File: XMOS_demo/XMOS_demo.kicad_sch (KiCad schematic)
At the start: 0 parts

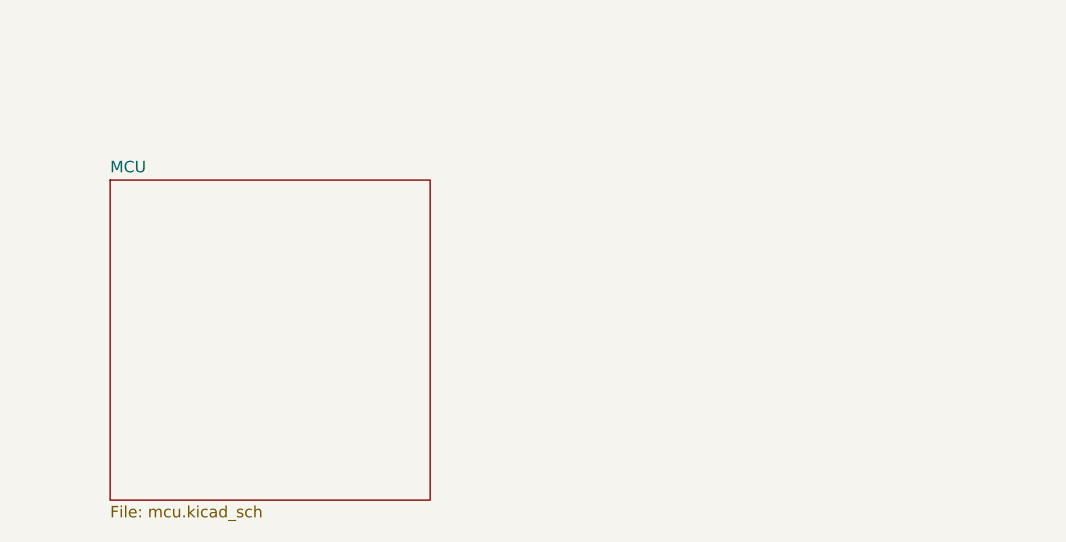
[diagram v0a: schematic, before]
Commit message: usb moved to seperate sch, power supply sch started
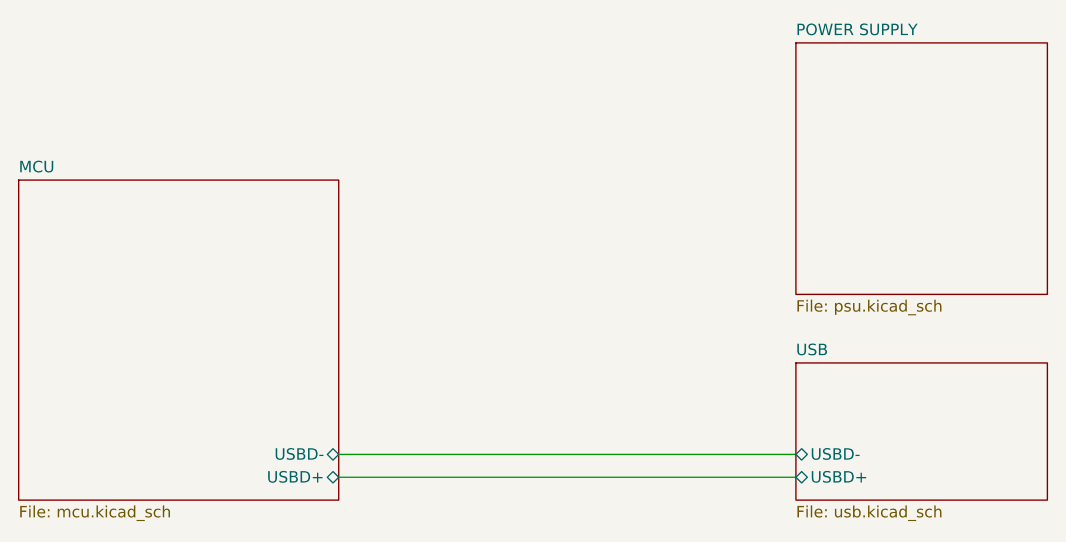
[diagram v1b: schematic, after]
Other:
- added sheet POWER SUPPLY (psu.kicad_sch)
- added sheet USB (usb.kicad_sch)
- sheet MCU ports: added USBD+, USBD-; removed none
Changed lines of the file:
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@@
 	(generator_version "9.0")
 	(paper "A4")
+	(wire
+		(pts
+			(xy 152.4 106.68) (xy 203.2 106.68)
+		)
+		(stroke
+			(width 0)
+			(type default)
+		)
+	)
+	(wire
+		(pts
+			(xy 152.4 109.22) (xy 203.2 109.22)
+		)
+		(stroke
+			(width 0)
+			(type default)
+		)
+	)
 	(sheet
-		(at 127 76.2)
+		(at 203.2 96.52)
+		(size 27.94 15.24)
+		(exclude_from_sim no)
+		(in_bom yes)
+		(on_board yes)
+		(dnp no)
+		(fields_autoplaced yes)
+		(stroke
+			(width 0.1524)
+			(type solid)
+		)
+		(fill
+			(color 0 0 0 0.0000)
+		)
+		(property "Sheetname" "USB"
+			(at 203.2 95.8084 0)
+			(effects
+				(font
+					(size 1.27 1.27)
+				)
+				(justify left bottom)
+			)
+		)
+		(property "Sheetfile" "usb.kicad_sch"
+			(at 203.2 112.3446 0)
+			(effects
+				(font
+					(size 1.27 1.27)
+				)
+				(justify left top)
+			)
+		)
+		(pin "USBD+" bidirectional
+			(at 203.2 109.22 180)
+			(effects
+				(font
+					(size 1.27 1.27)
+				)
+				(justify left)
+			)
+		)
+		(pin "USBD-" bidirectional
+			(at 203.2 106.68 180)
+			(effects
+				(font
+					(size 1.27 1.27)
+				)
+				(justify left)
+			)
+		)
+		(instances
+			(project "XMOS_demo"
+				(path "/0a855fb0-ca19-4770-811e-70d8770d7fdd"
+					(page "3")
+				)
+			)
+		)
+	)
+	(sheet
+		(at 203.2 60.96)
+		(size 27.94 27.94)
+		(exclude_from_sim no)
+		(in_bom yes)
+		(on_board yes)
+		(dnp no)
+		(fields_autoplaced yes)
+		(stroke
+			(width 0.1524)
+			(type solid)
+		)
+		(fill
+			(color 0 0 0 0.0000)
+		)
+		(property "Sheetname" "POWER SUPPLY"
+			(at 203.2 60.2484 0)
+			(effects
+				(font
+					(size 1.27 1.27)
+				)
+				(justify left bottom)
+			)
+		)
+		(property "Sheetfile" "psu.kicad_sch"
+			(at 203.2 89.4846 0)
+			(effects
+				(font
+					(size 1.27 1.27)
+				)
+				(justify left top)
+			)
+		)
+		(instances
+			(project "XMOS_demo"
+				(path "/0a855fb0-ca19-4770-811e-70d8770d7fdd"
+					(page "4")
+				)
+			)
+		)
+	)
+	(sheet
+		(at 116.84 76.2)
 		(size 35.56 35.56)
 		(exclude_from_sim no)
@@
 		)
 		(property "Sheetname" "MCU"
-			(at 127 75.4884 0)
+			(at 116.84 75.4884 0)
 			(effects
 				(font
@@
 		)
 		(property "Sheetfile" "mcu.kicad_sch"
-			(at 127 112.3446 0)
+			(at 116.84 112.3446 0)
 			(effects
 				(font
@@
 			)
 		)
+		(pin "USBD+" bidirectional
+			(at 152.4 109.22 0)
+			(effects
+				(font
+					(size 1.27 1.27)
+				)
+				(justify right)
+			)
+		)
+		(pin "USBD-" bidirectional
+			(at 152.4 106.68 0)
+			(effects
+				(font
+					(size 1.27 1.27)
+				)
+				(justify right)
+			)
+		)

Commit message: sch work
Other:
- added sheet Audio Out (audio_out.kicad_sch)
- added sheet Codec (codec.kicad_sch)
- company: (none) -> AGH University
- title: (none) -> USB Sound Card Top Level
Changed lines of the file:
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@@
 	(generator_version "9.0")
 	(paper "A4")
+	(title_block
+		(title "USB Sound Card Top Level")
+		(date "2026-03-29")
+		(rev "0.1")
+		(company "AGH University")
+	)
 	(wire
 		(pts
-			(xy 152.4 106.68) (xy 203.2 106.68)
+			(xy 107.95 109.22) (xy 116.84 109.22)
 		)
 		(stroke
@@
 	(wire
 		(pts
-			(xy 152.4 109.22) (xy 203.2 109.22)
+			(xy 107.95 106.68) (xy 116.84 106.68)
 		)
 		(stroke
@@
 	)
 	(sheet
-		(at 203.2 96.52)
+		(at 80.01 96.52)
 		(size 27.94 15.24)
 		(exclude_from_sim no)
@@
 		)
 		(property "Sheetname" "USB"
-			(at 203.2 95.8084 0)
+			(at 80.01 95.8084 0)
 			(effects
 				(font
@@
 		)
 		(property "Sheetfile" "usb.kicad_sch"
-			(at 203.2 112.3446 0)
+			(at 80.01 112.3446 0)
 			(effects
 				(font
@@
 		)
 		(pin "USBD+" bidirectional
-			(at 203.2 109.22 180)
-			(effects
-				(font
-					(size 1.27 1.27)
-				)
-				(justify left)
+			(at 107.95 109.22 0)
+			(effects
+				(font
+					(size 1.27 1.27)
+				)
+				(justify right)
 			)
 		)
 		(pin "USBD-" bidirectional
-			(at 203.2 106.68 180)
-			(effects
-				(font
-					(size 1.27 1.27)
-				)
-				(justify left)
+			(at 107.95 106.68 0)
+			(effects
+				(font
+					(size 1.27 1.27)
+				)
+				(justify right)
 			)
 		)
@@
 	)
 	(sheet
-		(at 203.2 60.96)
+		(at 80.01 55.88)
 		(size 27.94 27.94)
 		(exclude_from_sim no)
@@
 		)
 		(property "Sheetname" "POWER SUPPLY"
-			(at 203.2 60.2484 0)
+			(at 80.01 55.1684 0)
 			(effects
 				(font
@@
 		)
 		(property "Sheetfile" "psu.kicad_sch"
-			(at 203.2 89.4846 0)
+			(at 80.01 84.4046 0)
 			(effects
 				(font
@@
 				(path "/0a855fb0-ca19-4770-811e-70d8770d7fdd"
 					(page "4")
+				)
+			)
+		)
+	)
+	(sheet
+		(at 162.56 76.2)
+		(size 38.1 35.56)
+		(exclude_from_sim no)
+		(in_bom yes)
+		(on_board yes)
+		(dnp no)
+		(fields_autoplaced yes)
+		(stroke
+			(width 0.1524)
+			(type solid)
+		)
+		(fill
+			(color 0 0 0 0.0000)
+		)
+		(property "Sheetname" "Codec"
+			(at 162.56 75.4884 0)
+			(effects
+				(font
+					(size 1.27 1.27)
+				)
+				(justify left bottom)
+			)
+		)
+		(property "Sheetfile" "codec.kicad_sch"
+			(at 162.56 112.3446 0)
+			(effects
+				(font
+					(size 1.27 1.27)
+				)
+				(justify left top)
+			)
+		)
+		(instances
+			(project "XMOS_demo"
+				(path "/0a855fb0-ca19-4770-811e-70d8770d7fdd"
+					(page "6")
+				)
+			)
+		)
+	)
+	(sheet
+		(at 208.28 76.2)
+		(size 30.48 35.56)
+		(exclude_from_sim no)
+		(in_bom yes)
+		(on_board yes)
+		(dnp no)
+		(fields_autoplaced yes)
+		(stroke
+			(width 0.1524)
+			(type solid)
+		)
+		(fill
+			(color 0 0 0 0.0000)
+		)
+		(property "Sheetname" "Audio Out"
+			(at 208.28 75.4884 0)
+			(effects
+				(font
+					(size 1.27 1.27)
+				)
+				(justify left bottom)
+			)
+		)
+		(property "Sheetfile" "audio_out.kicad_sch"
+			(at 208.28 112.3446 0)
+			(effects
+				(font
+					(size 1.27 1.27)
+				)
+				(justify left top)
+			)
+		)
+		(instances
+			(project "XMOS_demo"
+				(path "/0a855fb0-ca19-4770-811e-70d8770d7fdd"
+					(page "5")
 				)
 			)
@@
 		)
 		(pin "USBD+" bidirectional
-			(at 152.4 109.22 0)
-			(effects
-				(font
-					(size 1.27 1.27)
-				)
-				(justify right)
+			(at 116.84 109.22 180)
+			(effects
+				(font
+					(size 1.27 1.27)
+				)
+				(justify left)
 			)
 		)
 		(pin "USBD-" bidirectional
-			(at 152.4 106.68 0)
-			(effects
-				(font
-					(size 1.27 1.27)
-				)
-				(justify right)
-			)
-		)
+			(at 116.84 106.68 180)
+			(effects
+				(font
+					(size 1.27 1.27)
+				)
+				(justify left)
+			)
+		)

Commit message: Lots of sch work
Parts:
- added NT1, NT2, NT3, NT4, NT5: NetTie_2, NetTie:NetTie-2_SMD_Pad0.5mm, symbol Device:NetTie_2
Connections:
- new net Audio Out/INL+: NT4.2
- new net Audio Out/INL-: NT5.2
- new net Audio Out/INR+: NT2.2
- new net Audio Out/INR-: NT3.2
- new net Audio Out/~{SHDN}: NT1.2
- new net Codec/OUT_A+: NT2.1
- new net Codec/OUT_A-: NT3.1
- new net Codec/OUT_B+: NT4.1
- new net Codec/OUT_B-: NT5.1
- new net Codec/~{MUTE}: NT1.1
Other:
- sheet Audio Out ports: added INL+, INL-, INR+, INR-, ~{SHDN}; removed none
- sheet Codec ports: added AIN_A, AIN_B, OUT_A+, OUT_A-, OUT_B+, OUT_B-, VQ1, VQ2, VQ3, ~{MUTE}; removed none
- note added: "TODO: add audio input front end"
- note added: "TODO: add optional low pass filter"

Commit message: sch work, pcb import and initial board outline
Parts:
- added H1, H2, H3, H4: M3_NPTH, MountingHole:MountingHole_3.2mm_M3, symbol Mechanical:MountingHole
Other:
- added sheet Audio In (audio_in.kicad_sch)
- sheet Codec ports: added CODEC_LRCK, CODEC_MCLK, CODEC_SCLK, CODEC_SDIN, CODEC_SDOUT, CODEC_~{RST}, SCL, SDA; removed none
- note added: "TODO: add missing voltage regulators"

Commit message: sch mostly finished, needs tp, pcb component layout started
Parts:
- added TP1, TP2, TP3, TP4: GND, TestPoint:TestPoint_Bridge_Pitch2.54mm_Drill1.0mm, symbol Connector:TestPoint
- renumbered NT2 to NT1, NT3 to NT2, NT4 to NT3, NT5 to NT4, NT1 to NT5
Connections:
- net Audio Out/INL+: now also NT1.2; no longer NT3.2
- net Audio Out/INL-: now also NT2.2; no longer NT4.2
- net Audio Out/INR+: now also NT3.2; no longer NT1.2
- net Audio Out/INR-: now also NT4.2; no longer NT2.2
- new net GND: TP1.1, TP2.1, TP3.1, TP4.1
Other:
- sheet Audio In ports: added AIN_A, AIN_B, VQ1, VQ2, VQ3; removed none
- note removed: "TODO: add audio input front end"
- note removed: "TODO: add missing voltage regulators"

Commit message: finished sch, pcb work
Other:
- sheet Codec ports: added I2S_ADC, I2S_DAC, I2S_LRCK, I2S_SCLK, MCLK; removed CODEC_LRCK, CODEC_MCLK, CODEC_SCLK, CODEC_SDIN, CODEC_SDOUT
- sheet MCU ports: added CODEC_~{RST}, I2S_ADC, I2S_DAC, I2S_LRCK, I2S_SCLK, MCLK, SCL, SDA; removed none
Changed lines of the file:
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@@
+	(wire
+		(pts
+			(xy 119.38 88.9) (xy 129.54 88.9)
+		)
+		(stroke
+			(width 0)
+			(type default)
+		)
+	)
+	(wire
+		(pts
+			(xy 119.38 91.44) (xy 129.54 91.44)
+		)
+		(stroke
+			(width 0)
+			(type default)
+		)
+	)
 	(wire
 		(pts
@@
 	(wire
 		(pts
+			(xy 119.38 109.22) (xy 129.54 109.22)
+		)
+		(stroke
+			(width 0)
+			(type default)
+		)
+	)
+	(wire
+		(pts
 			(xy 167.64 83.82) (xy 175.26 83.82)
 		)
@@
 	(wire
 		(pts
+			(xy 119.38 93.98) (xy 129.54 93.98)
+		)
+		(stroke
+			(width 0)
+			(type default)
+		)
+	)
+	(wire
+		(pts
 			(xy 45.72 129.54) (xy 35.56 129.54)
 		)
@@
 	(wire
 		(pts
+			(xy 119.38 86.36) (xy 129.54 86.36)
+		)
+		(stroke
+			(width 0)
+			(type default)
+		)
+	)
+	(wire
+		(pts
 			(xy 167.64 81.28) (xy 175.26 81.28)
 		)
@@
 	(wire
 		(pts
+			(xy 119.38 106.68) (xy 129.54 106.68)
+		)
+		(stroke
+			(width 0)
+			(type default)
+		)
+	)
+	(wire
+		(pts
+			(xy 119.38 96.52) (xy 129.54 96.52)
+		)
+		(stroke
+			(width 0)
+			(type default)
+		)
+	)
+	(wire
+		(pts
 			(xy 74.93 109.22) (xy 83.82 109.22)
 		)
@@
 		(pts
 			(xy 180.34 78.74) (xy 213.36 78.74)
+		)
+		(stroke
+			(width 0)
+			(type default)
+		)
+	)
+	(wire
+		(pts
+			(xy 119.38 78.74) (xy 129.54 78.74)
 		)
 		(stroke
@@
 		(dnp no)
 		(fields_autoplaced yes)
-		(property "Reference" "#PWR094"
+		(property "Reference" "#PWR01"
 			(at 35.56 138.43 0)
 			(effects
@@
 			(project "XMOS_demo"
 				(path "/0a855fb0-ca19-4770-811e-70d8770d7fdd"
-					(reference "#PWR094")
+					(reference "#PWR01")
 					(unit 1)
 				)
@@
 			)
 		)
-		(pin "CODEC_LRCK" input
+		(pin "I2S_ADC" output
 			(at 129.54 88.9 180)
 			(effects
@@
 			)
 		)
-		(pin "CODEC_MCLK" input
+		(pin "MCLK" input
 			(at 129.54 86.36 180)
 			(effects
@@
 			)
 		)
-		(pin "CODEC_SCLK" input
+		(pin "I2S_SCLK" input
 			(at 129.54 91.44 180)
 			(effects
@@
 			)
 		)
-		(pin "CODEC_SDIN" input
+		(pin "I2S_DAC" input
 			(at 129.54 96.52 180)
 			(effects
@@
 			)
 		)
-		(pin "CODEC_SDOUT" output
+		(pin "I2S_LRCK" input
 			(at 129.54 93.98 180)
 			(effects
@@
 			)
 		)
+		(pin "CODEC_~{RST}" output
+			(at 119.38 78.74 0)
+			(effects
+				(font
+					(size 1.27 1.27)
+				)
+				(justify right)
+			)
+		)
+		(pin "I2S_ADC" input
+			(at 119.38 88.9 0)
+			(effects
+				(font
+					(size 1.27 1.27)
+				)
+				(justify right)
+			)
+		)
+		(pin "I2S_SCLK" output
+			(at 119.38 91.44 0)
+			(effects
+				(font
+					(size 1.27 1.27)
+				)
+				(justify right)
+			)
+		)
+		(pin "I2S_DAC" output
+			(at 119.38 96.52 0)
+			(effects
+				(font
+					(size 1.27 1.27)
+				)
+				(justify right)
+			)
+		)
+		(pin "I2S_LRCK" output
+			(at 119.38 93.98 0)
+			(effects
+				(font
+					(size 1.27 1.27)
+				)
+				(justify right)
+			)
+		)
+		(pin "MCLK" output
+			(at 119.38 86.36 0)
+			(effects
+				(font
+					(size 1.27 1.27)
+				)
+				(justify right)
+			)
+		)
+		(pin "SCL" bidirectional
+			(at 119.38 106.68 0)
+			(effects
+				(font
+					(size 1.27 1.27)
+				)
+				(justify right)
+			)
+		)
+		(pin "SDA" bidirectional
+			(at 119.38 109.22 0)
+			(effects
+				(font
+					(size 1.27 1.27)
+				)
+				(justify right)
+			)
+		)

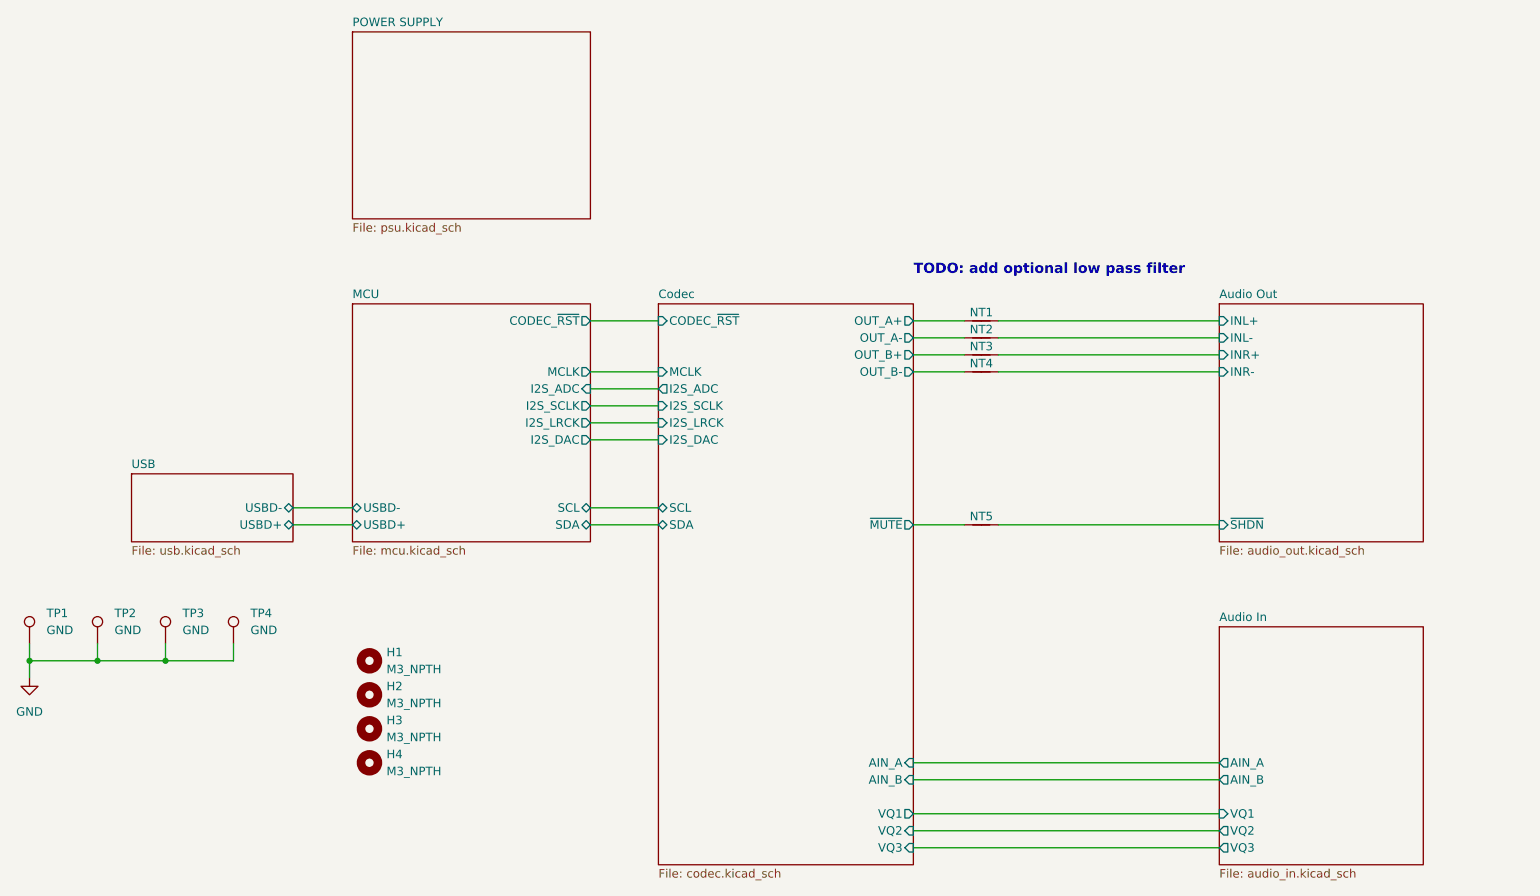
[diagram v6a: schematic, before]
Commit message: sch work changes (jumpers, connectors, tp)
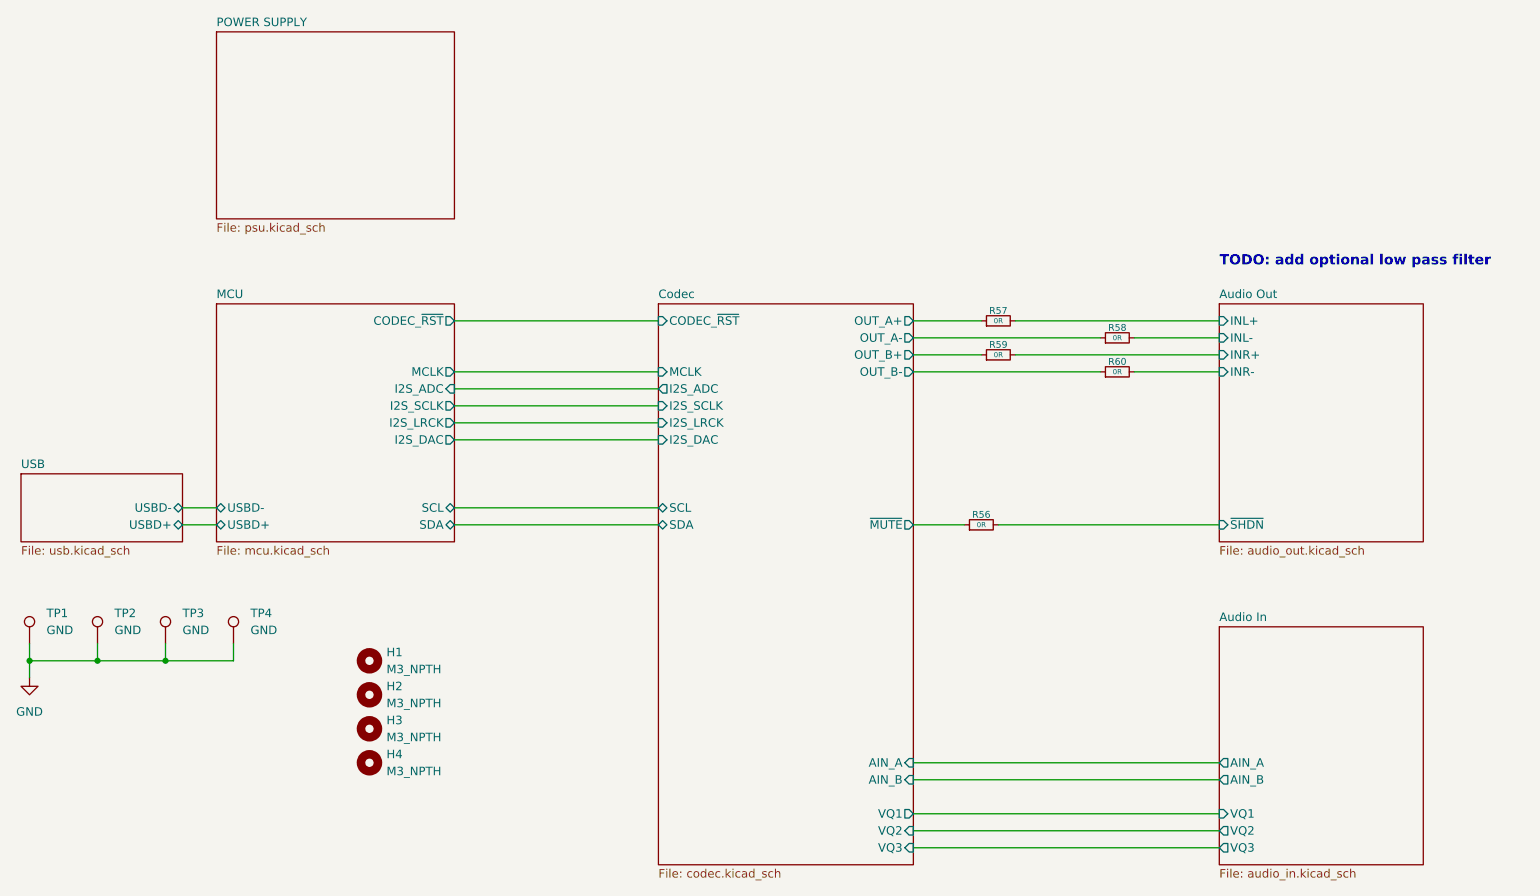
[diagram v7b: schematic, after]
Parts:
- removed NT1, NT2, NT3, NT4, NT5: NetTie_2, NetTie:NetTie-2_SMD_Pad0.5mm, symbol Device:NetTie_2
- added R56, R57, R58, R59, R60: 0R, Resistor_SMD:R_0603_1608Metric, symbol Device:R_Small
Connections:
- net Audio Out/INL+: now also R57.2
- net Audio Out/INL-: now also R58.2
- net Audio Out/INR+: now also R59.2
- net Audio Out/INR-: now also R60.2
- net Audio Out/~{SHDN}: now also R56.2
- net Codec/OUT_A+: now also R57.1
- net Codec/OUT_A-: now also R58.1
- net Codec/OUT_B+: now also R59.1
- net Codec/OUT_B-: now also R60.1
- net Codec/~{MUTE}: now also R56.1

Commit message: pcb routing
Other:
- sheet Audio In ports: added VQ2_3; removed VQ2, VQ3
- sheet Codec ports: added VQ2_3; removed VQ2, VQ3
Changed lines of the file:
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@@
-	(wire
-		(pts
-			(xy 167.64 157.48) (xy 213.36 157.48)
-		)
-		(stroke
-			(width 0)
-			(type default)
-		)
-	)
 	(wire
 		(pts
@@
 			)
 		)
-		(pin "VQ2" input
+		(pin "VQ2_3" input
 			(at 167.64 154.94 0)
-			(effects
-				(font
-					(size 1.27 1.27)
-				)
-				(justify right)
-			)
-		)
-		(pin "VQ3" input
-			(at 167.64 157.48 0)
 			(effects
 				(font
@@
 			)
 		)
-		(pin "VQ2" output
+		(pin "VQ2_3" output
 			(at 213.36 154.94 180)
 			(effects
 				(font
-					(size 1.27 1.27)
-				)
-				(justify left)
-			)
-		)
-		(pin "VQ3" output
-			(at 213.36 157.48 180)
-			(effects
-				(font
